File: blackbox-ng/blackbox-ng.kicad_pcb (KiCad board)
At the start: 2 copper layers, 48.3 x 43.2 mm, 50 parts, among them J1 CONN_DEBUG, J2 JST_PH, J3 CARD1, J4 CARD2, J5 Conn_01x08, J6 UART, SW1 SW_Push, SW2 SW_Push, U1 AP2112K-3.3, U2 STM32F401RETx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

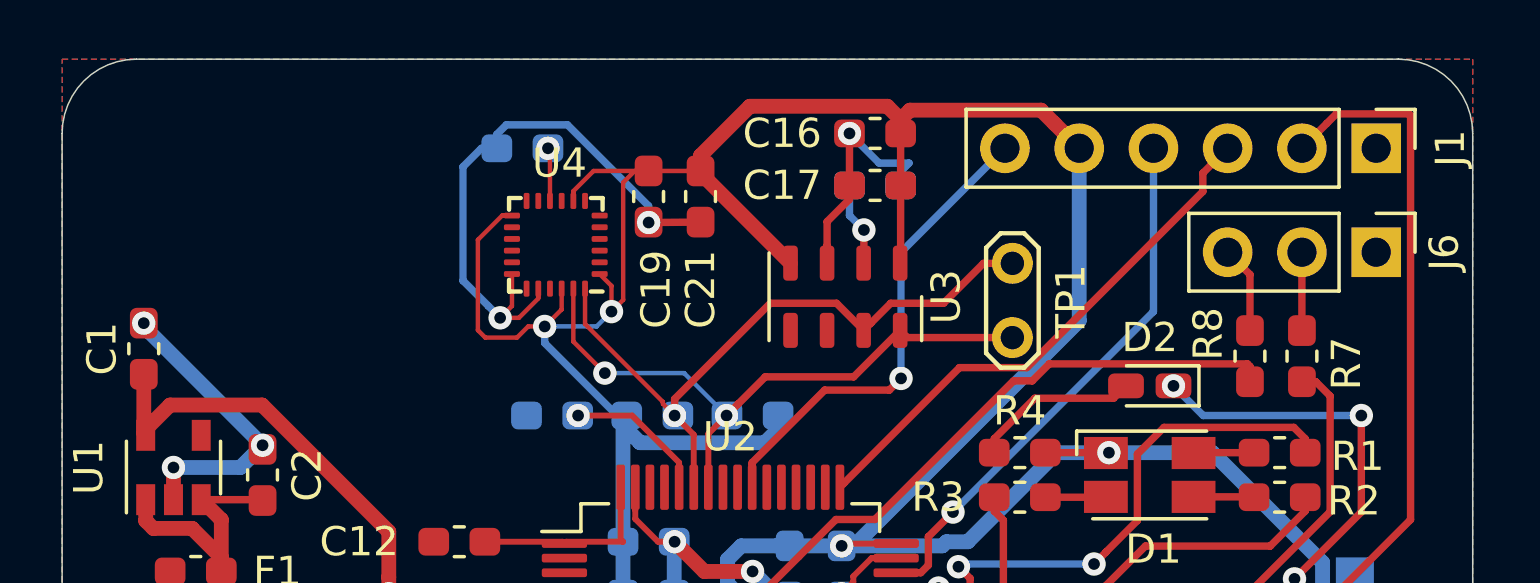
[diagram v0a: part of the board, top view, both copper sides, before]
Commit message: add logos
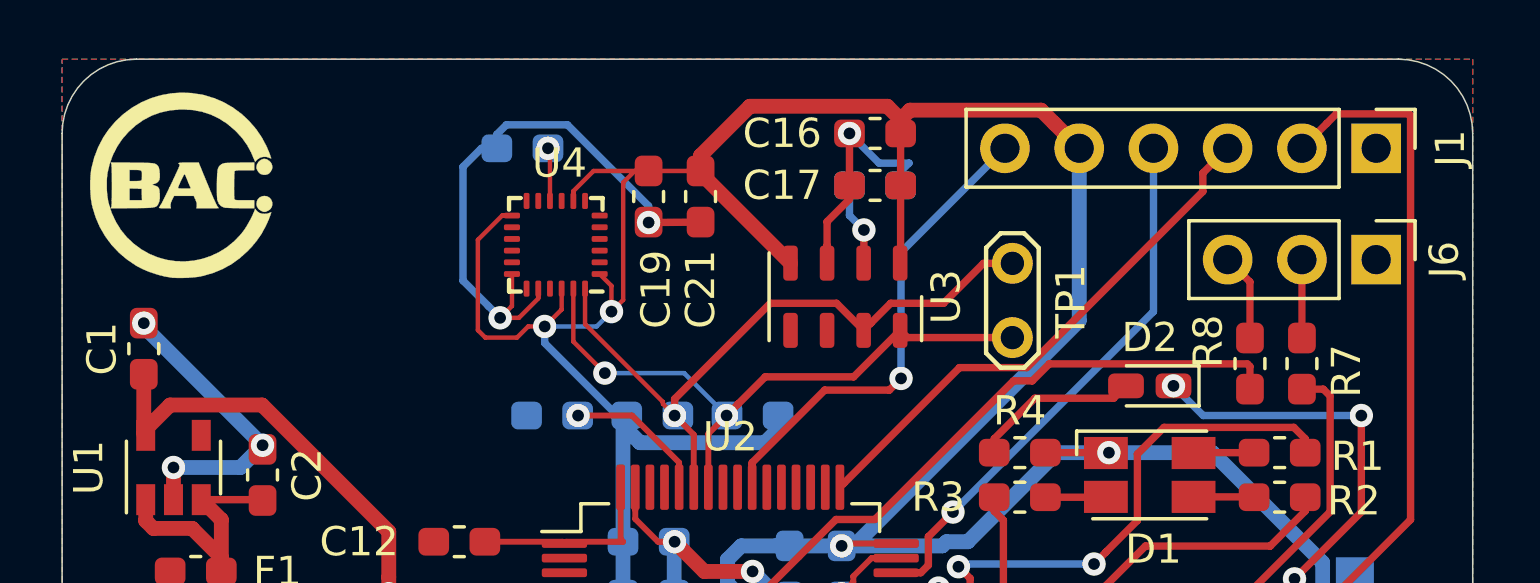
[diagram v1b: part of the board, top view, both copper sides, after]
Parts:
- added G***: LOGO, FLOOF:star, F.Cu at (137.7, 80.8)
- added G***: LOGO, FLOOF:bac, F.Cu at (131.1, 80.5)
- moved J6 0.25 mm to (172.0, 83.1)
- moved R7 0.25 mm to (169.4, 86.6)
- moved R8 0.25 mm to (167.6, 86.6)
